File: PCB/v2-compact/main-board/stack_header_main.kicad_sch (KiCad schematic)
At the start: 0 parts

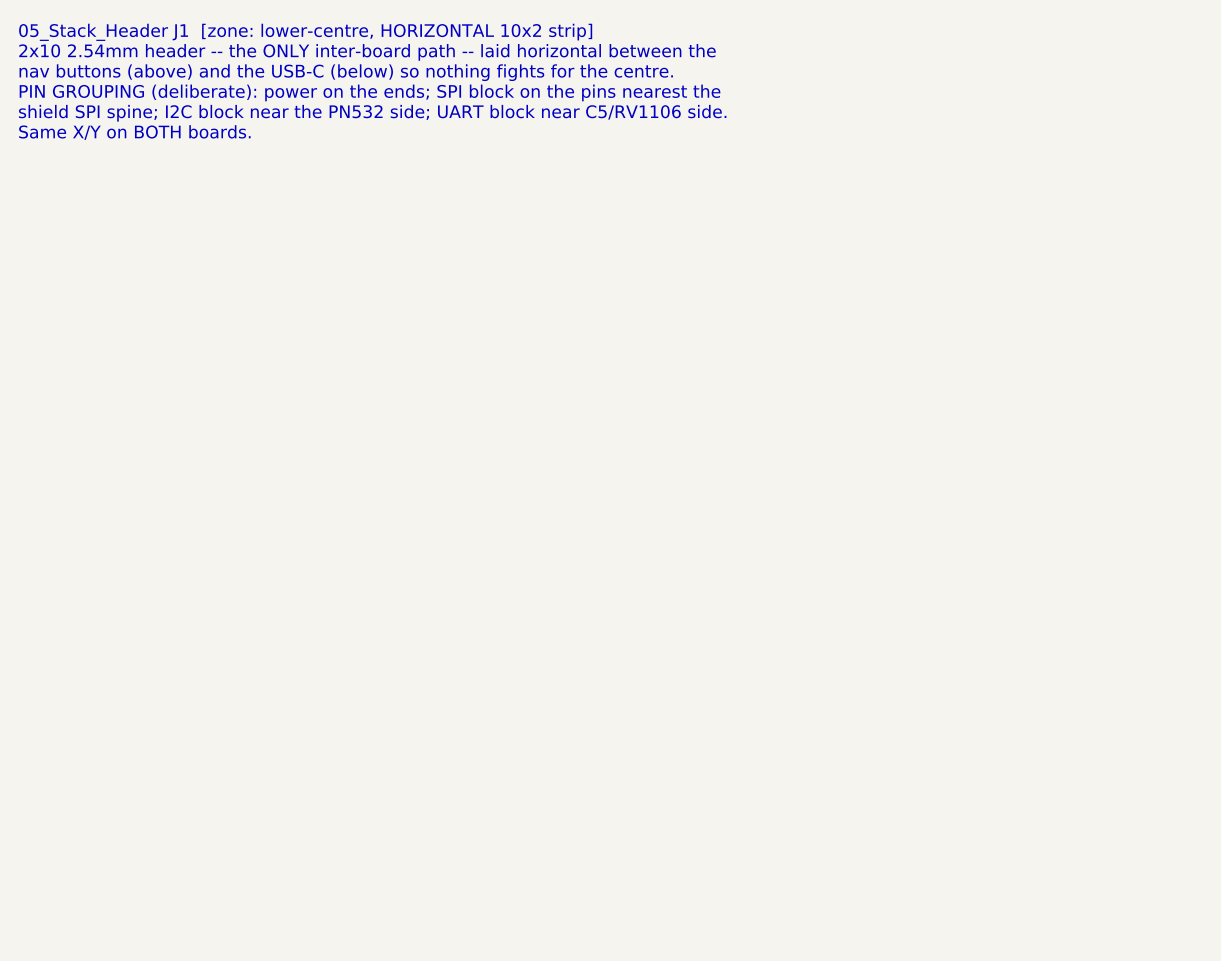
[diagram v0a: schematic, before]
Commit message: Schematics: custom symbols + footprint lib + backbone/nRF24/iButton sheets
- Add SnowOwl.kicad_sym (nRF24 + CC1101 module symbols; MISO tri-state for the
  shared SPI bus) and SnowOwl.pretty with the 2x10 stack-header footprint,
  registered via project sym-lib-table / fp-lib-table on both boards.
- Capture sheets, each netlist- and ERC-checked:
  - J1 stack header (both boards) wired to the locked pinout (the interconnect
    backbone: power + I2C + S3<->C5 UART + S3<->RV1106 UART + IR + 1-Wire)
  - nRF24 x3 on the shared SPI spine (per-radio CE/CSN/IRQ) with decoupling
  - iButton 1-Wire with pull-up
- Engine: snap all placements to the 1.27mm grid (clears 103 off-grid warnings);
  globally-unique power-symbol refs.

Remaining ERC items are expected for a partial design (isolated labels resolve
when both ends of a net are captured; power-not-driven clears with the power sheet).
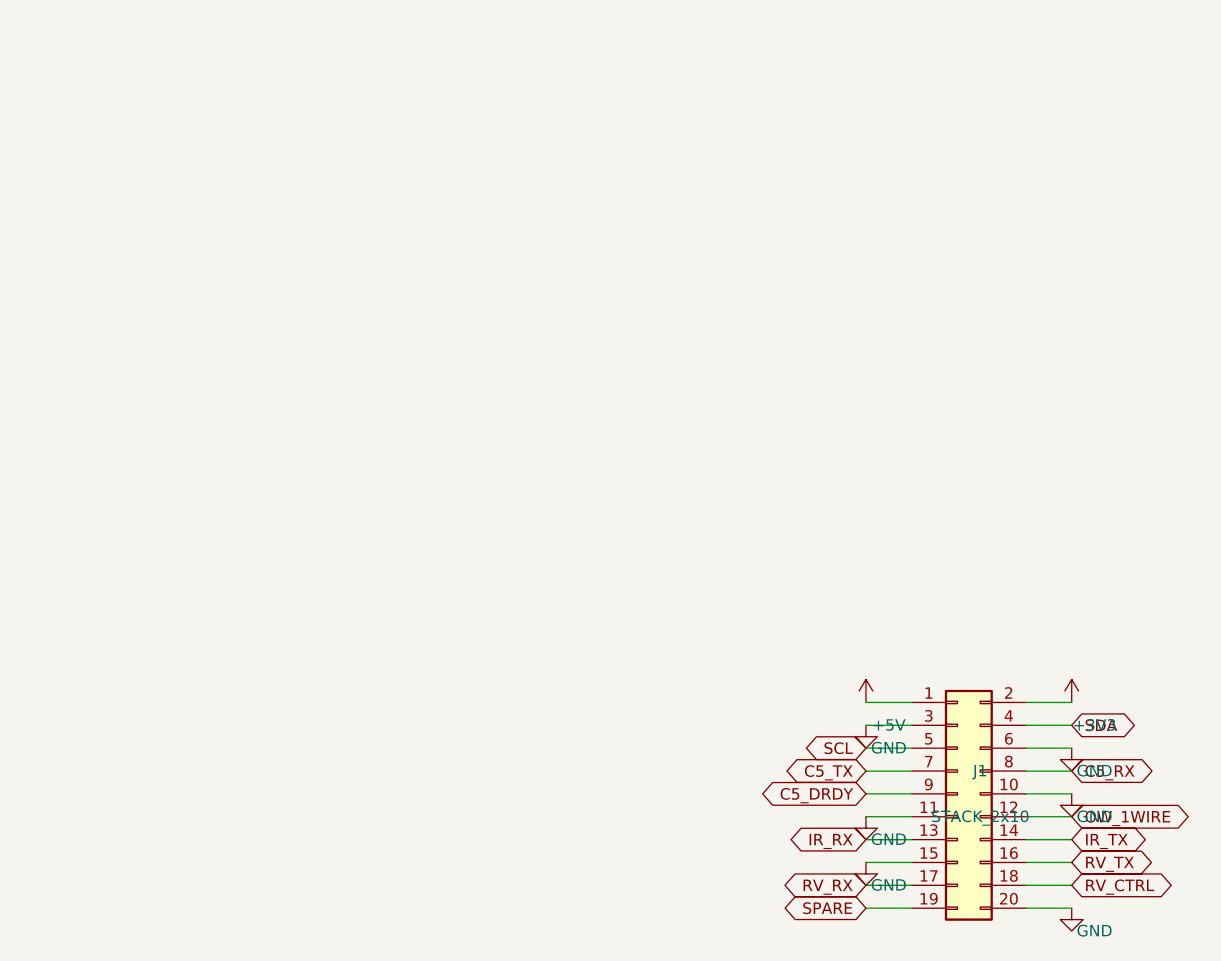
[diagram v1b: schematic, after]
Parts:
- added J1: STACK_2x10, SnowOwl:StackHeader_2x10, symbol Connector_Generic:Conn_02x10_Odd_Even
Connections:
- new net +3V3: J1.2 (Pin_2)
- new net +5V: J1.1 (Pin_1)
- new net C5_DRDY: J1.9 (Pin_9)
- new net C5_RX: J1.8 (Pin_8)
- new net C5_TX: J1.7 (Pin_7)
- new net GND: J1.10 (Pin_10), J1.11 (Pin_11), J1.15 (Pin_15), J1.20 (Pin_20), J1.3 (Pin_3), J1.6 (Pin_6)
- new net IR_RX: J1.13 (Pin_13)
- new net IR_TX: J1.14 (Pin_14)
- new net OW_1WIRE: J1.12 (Pin_12)
- new net RV_CTRL: J1.18 (Pin_18)
- new net RV_RX: J1.17 (Pin_17)
- new net RV_TX: J1.16 (Pin_16)
- new net SCL: J1.5 (Pin_5)
- new net SDA: J1.4 (Pin_4)
- new net SPARE: J1.19 (Pin_19)
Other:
- note removed: "05_Stack_Header J1 [zone: lower-centre, HORIZONTAL 10x2 strip] 2x10 2.54mm header -- the ONLY inter-board path -- laid horizontal between the nav buttons (above) and the USB-C (below) so nothing fights for the centre. PIN GROUPING (deliberate): power on the ends; SPI block on the pins nearest the shield SPI spine; I2C block near the PN532 side; UART block near C5/RV1106 side. Same X/Y on BOTH boa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"
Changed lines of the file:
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@@
   (paper "A4")
   (title_block (title "05_Stack_Header") (company "YurilLAB"))
-  (text "05_Stack_Header J1  [zone: lower-centre, HORIZONTAL 10x2 strip]
-2x10 2.54mm header -- the ONLY inter-board path -- laid horizontal between the
-nav buttons (above) and the USB-C (below) so nothing fights for the centre.
-PIN GROUPING (deliberate): power on the ends; SPI block on the pins nearest the
-shield SPI spine; I2C block near the PN532 side; UART block near C5/RV1106 side.
-Same X/Y on BOTH boards." (at 15 15 0)
-    (effects (font (size 1.4 1.4)) (justify left top)))
+  (symbol (lib_id "Connector_Generic:Conn_02x10_Odd_Even") (at 119.38 100.33 0) (unit 1)
+    (in_bom yes) (on_board yes) (dnp no)
+    (property "Reference" "J1" (at 121.92 97.79 0) (effects (font (size 1.27 1.27))))
+    (property "Value" "STACK_2x10" (at 121.92 102.87 0) (effects (font (size 1.27 1.27))))
+    (property "Footprint" "SnowOwl:StackHeader_2x10" (at 119.38 100.33 0) (effects (font (size 1.27 1.27)) hide))
+    (pin "1")
+    (pin "2")
+    (pin "3")
+    (pin "4")
+    (pin "5")
+    (pin "6")
+    (pin "7")
+    (pin "8")
+    (pin "9")
+    (pin "10")
+    (pin "11")
+    (pin "12")
+    (pin "13")
+    (pin "14")
+    (pin "15")
+    (pin "16")
+    (pin "17")
+    (pin "18")
+    (pin "19")
+    (pin "20")
+    (instances (project "SnowOwl-Main" (path "/a1b2c3d4-0001-4001-8001-000000000015" (reference "J1") (unit 1))))
+  )
+  (wire (pts (xy 114.3 90.17) (xy 109.22 90.17)) (stroke (width 0) (type default)))
+  (symbol (lib_id "power:+5V") (at 109.22 90.17 0) (unit 1)
+    (in_bom yes) (on_board yes) (dnp no)
+    (property "Reference" "#PWR1C7936E" (at 111.76 87.63 0) (effects (font (size 1.27 1.27)) hide))
+    (property "Value" "+5V" (at 111.76 92.71 0) (effects (font (size 1.27 1.27))))
+    (property "Footprint" "" (at 109.22 90.17 0) (effects (font (size 1.27 1.27)) hide))
+    (pin "1")
+    (instances (project "SnowOwl-Main" (path "/a1b2c3d4-0001-4001-8001-000000000015" (reference "#PWR1C7936E") (unit 1))))
+  )
+  (wire (pts (xy 127 90.17) (xy 132.08 90.17)) (stroke (width 0) (type default)))
+  (symbol (lib_id "power:+3V3") (at 132.08 90.17 0) (unit 1)
+    (in_bom yes) (on_board yes) (dnp no)
+    (property "Reference" "#PWR5F75EBB" (at 134.62 87.63 0) (effects (font (size 1.27 1.27)) hide))
+    (property "Value" "+3V3" (at 134.62 92.71 0) (effects (font (size 1.27 1.27))))
+    (property "Footprint" "" (at 132.08 90.17 0) (effects (font (size 1.27 1.27)) hide))
+    (pin "1")
+    (instances (project "SnowOwl-Main" (path "/a1b2c3d4-0001-4001-8001-000000000015" (reference "#PWR5F75EBB") (unit 1))))
+  )
+  (wire (pts (xy 114.3 92.71) (xy 109.22 92.71)) (stroke (width 0) (type default)))
+  (symbol (lib_id "power:GND") (at 109.22 92.71 0) (unit 1)
+    (in_bom yes) (on_board yes) (dnp no)
+    (property "Reference" "#PWR3A53E75" (at 111.76 90.17 0) (effects (font (size 1.27 1.27)) hide))
+    (property "Value" "GND" (at 111.76 95.25 0) (effects (font (size 1.27 1.27))))
+    (property "Footprint" "" (at 109.22 92.71 0) (effects (font (size 1.27 1.27)) hide))
+    (pin "1")
+    (instances (project "SnowOwl-Main" (path "/a1b2c3d4-0001-4001-8001-000000000015" (reference "#PWR3A53E75") (unit 1))))
+  )
+  (wire (pts (xy 127 92.71) (xy 132.08 92.71)) (stroke (width 0) (type default)))
+  (global_label "SDA" (shape bidirectional) (at 132.08 92.71 0) (fields_autoplaced)
+    (effects (font (size 1.27 1.27)) (justify left)))
+  (wire (pts (xy 114.3 95.25) (xy 109.22 95.25)) (stroke (width 0) (type default)))
+  (global_label "SCL" (shape bidirectional) (at 109.22 95.25 180) (fields_autoplaced)
+    (effects (font (size 1.27 1.27)) (justify right)))
+  (wire (pts (xy 127 95.25) (xy 132.08 95.25)) (stroke (width 0) (type default)))
+  (symbol (lib_id "power:GND") (at 132.08 95.25 0) (unit 1)
+    (in_bom yes) (on_board yes) (dnp no)
+    (property "Reference" "#PWRA65B904" (at 134.62 92.71 0) (effects (font (size 1.27 1.27)) hide))
+    (property "Value" "GND" (at 134.62 97.79 0) (effects (font (size 1.27 1.27))))
+    (property "Footprint" "" (at 132.08 95.25 0) (effects (font (size 1.27 1.27)) hide))
+    (pin "1")
+    (instances (project "SnowOwl-Main" (path "/a1b2c3d4-0001-4001-8001-000000000015" (reference "#PWRA65B904") (unit 1))))
+  )
+  (wire (pts (xy 114.3 97.79) (xy 109.22 97.79)) (stroke (width 0) (type default)))
+  (global_label "C5_TX" (shape bidirectional) (at 109.22 97.79 180) (fields_autoplaced)
+    (effects (font (size 1.27 1.27)) (justify right)))
+  (wire (pts (xy 127 97.79) (xy 132.08 97.79)) (stroke (width 0) (type default)))
+  (global_label "C5_RX" (shape bidirectional) (at 132.08 97.79 0) (fields_autoplaced)
+    (effects (font (size 1.27 1.27)) (justify left)))
+  (wire (pts (xy 114.3 100.33) (xy 109.22 100.33)) (stroke (width 0) (type default)))
+  (global_label "C5_DRDY" (shape bidirectional) (at 109.22 100.33 180) (fields_autoplaced)
+    (effects (font (size 1.27 1.27)) (justify right)))
+  (wire (pts (xy 127 100.33) (xy 132.08 100.33)) (stroke (width 0) (type default)))
+  (symbol (lib_id "power:GND") (at 132.08 100.33 0) (unit 1)
+    (in_bom yes) (on_board yes) (dnp no)
+    (property "Reference" "#PWR0D64A24" (at 134.62 97.79 0) (effects (font (size 1.27 1.27)) hide))
+    (property "Value" "GND" (at 134.62 102.87 0) (effects (font (size 1.27 1.27))))
+    (property "Footprint" "" (at 132.08 100.33 0) (effects (font (size 1.27 1.27)) hide))
+    (pin "1")
+    (instances (project "SnowOwl-Main" (path "/a1b2c3d4-0001-4001-8001-000000000015" (reference "#PWR0D64A24") (unit 1))))
+  )
+  (wire (pts (xy 114.3 102.87) (xy 109.22 102.87)) (stroke (width 0) (type default)))
+  (symbol (lib_id "power:GND") (at 109.22 102.87 0) (unit 1)
+    (in_bom yes) (on_board yes) (dnp no)
+    (property "Reference" "#PWRE9AFCB3" (at 111.76 100.33 0) (effects (font (size 1.27 1.27)) hide))
+    (property "Value" "GND" (at 111.76 105.41 0) (effects (font (size 1.27 1.27))))
+    (property "Footprint" "" (at 109.22 102.87 0) (effects (font (size 1.27 1.27)) hide))
+    (pin "1")
+    (instances (project "SnowOwl-Main" (path "/a1b2c3d4-0001-4001-8001-000000000015" (reference "#PWRE9AFCB3") (unit 1))))
+  )
+  (wire (pts (xy 127 102.87) (xy 132.08 102.87)) (stroke (width 0) (type default)))
+  (global_label "OW_1WIRE" (shape bidirectional) (at 132.08 102.87 0) (fields_autoplaced)
+    (effects (font (size 1.27 1.27)) (justify left)))
+  (wire (pts (xy 114.3 105.41) (xy 109.22 105.41)) (stroke (width 0) (type default)))
+  (global_label "IR_RX" (shape bidirectional) (at 109.22 105.41 180) (fields_autoplaced)
+    (effects (font (size 1.27 1.27)) (justify right)))
+  (wire (pts (xy 127 105.41) (xy 132.08 105.41)) (stroke (width 0) (type default)))
+  (global_label "IR_TX" (shape bidirectional) (at 132.08 105.41 0) (fields_autoplaced)
+    (effects (font (size 1.27 1.27)) (justify left)))
+  (wire (pts (xy 114.3 107.95) (xy 109.22 107.95)) (stroke (width 0) (type default)))
+  (symbol (lib_id "power:GND") (at 109.22 107.95 0) (unit 1)
+    (in_bom yes) (on_board yes) (dnp no)
+    (property "Reference" "#PWR8A82442" (at 111.76 105.41 0) (effects (font (size 1.27 1.27)) hide))
+    (property "Value" "GND" (at 111.76 110.49 0) (effects (font (size 1.27 1.27))))
+    (property "Footprint" "" (at 109.22 107.95 0) (effects (font (size 1.27 1.27)) hide))
+    (pin "1")
+    (instances (project "SnowOwl-Main" (path "/a1b2c3d4-0001-4001-8001-000000000015" (reference "#PWR8A82442") (unit 1))))
+  )
+  (wire (pts (xy 127 107.95) (xy 132.08 107.95)) (stroke (width 0) (type default)))
+  (global_label "RV_TX" (shape bidirectional) (at 132.08 107.95 0) (fields_autoplaced)
+    (effects (font (size 1.27 1.27)) (justify left)))
+  (wire (pts (xy 114.3 110.49) (xy 109.22 110.49)) (stroke (width 0) (type default)))
+  (global_label "RV_RX" (shape bidirectional) (at 109.22 110.49 180) (fields_autoplaced)
+    (effects (font (size 1.27 1.27)) (justify right)))
+  (wire (pts (xy 127 110.49) (xy 132.08 110.49)) (stroke (width 0) (type default)))
+  (global_label "RV_CTRL" (shape bidirectional) (at 132.08 110.49 0) (fields_autoplaced)
+    (effects (font (size 1.27 1.27)) (justify left)))
+  (wire (pts (xy 114.3 113.03) (xy 109.22 113.03)) (stroke (width 0) (type default)))
+  (global_label "SPARE" (shape bidirectional) (at 109.22 113.03 180) (fields_autoplaced)
+    (effects (font (size 1.27 1.27)) (justify right)))
+  (wire (pts (xy 127 113.03) (xy 132.08 113.03)) (stroke (width 0) (type default)))
+  (symbol (lib_id "power:GND") (at 132.08 113.03 0) (unit 1)
+    (in_bom yes) (on_board yes) (dnp no)
+    (property "Reference" "#PWR72AA0D3" (at 134.62 110.49 0) (effects (font (size 1.27 1.27)) hide))
+    (property "Value" "GND" (at 134.62 115.57 0) (effects (font (size 1.27 1.27))))
+    (property "Footprint" "" (at 132.08 113.03 0) (effects (font (size 1.27 1.27)) hide))
+    (pin "1")
+    (instances (project "SnowOwl-Main" (path "/a1b2c3d4-0001-4001-8001-000000000015" (reference "#PWR72AA0D3") (unit 1))))
+  )
   (sheet_instances (path "/" (page "1")))
 )
